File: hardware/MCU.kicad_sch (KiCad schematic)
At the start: 26 parts, among them J1 Conn_01x03_Pin, SW1 SW_MEC_5G, U1 STM32G473QETxZ, U2 IS61W204816BLL, Y1 25MHz

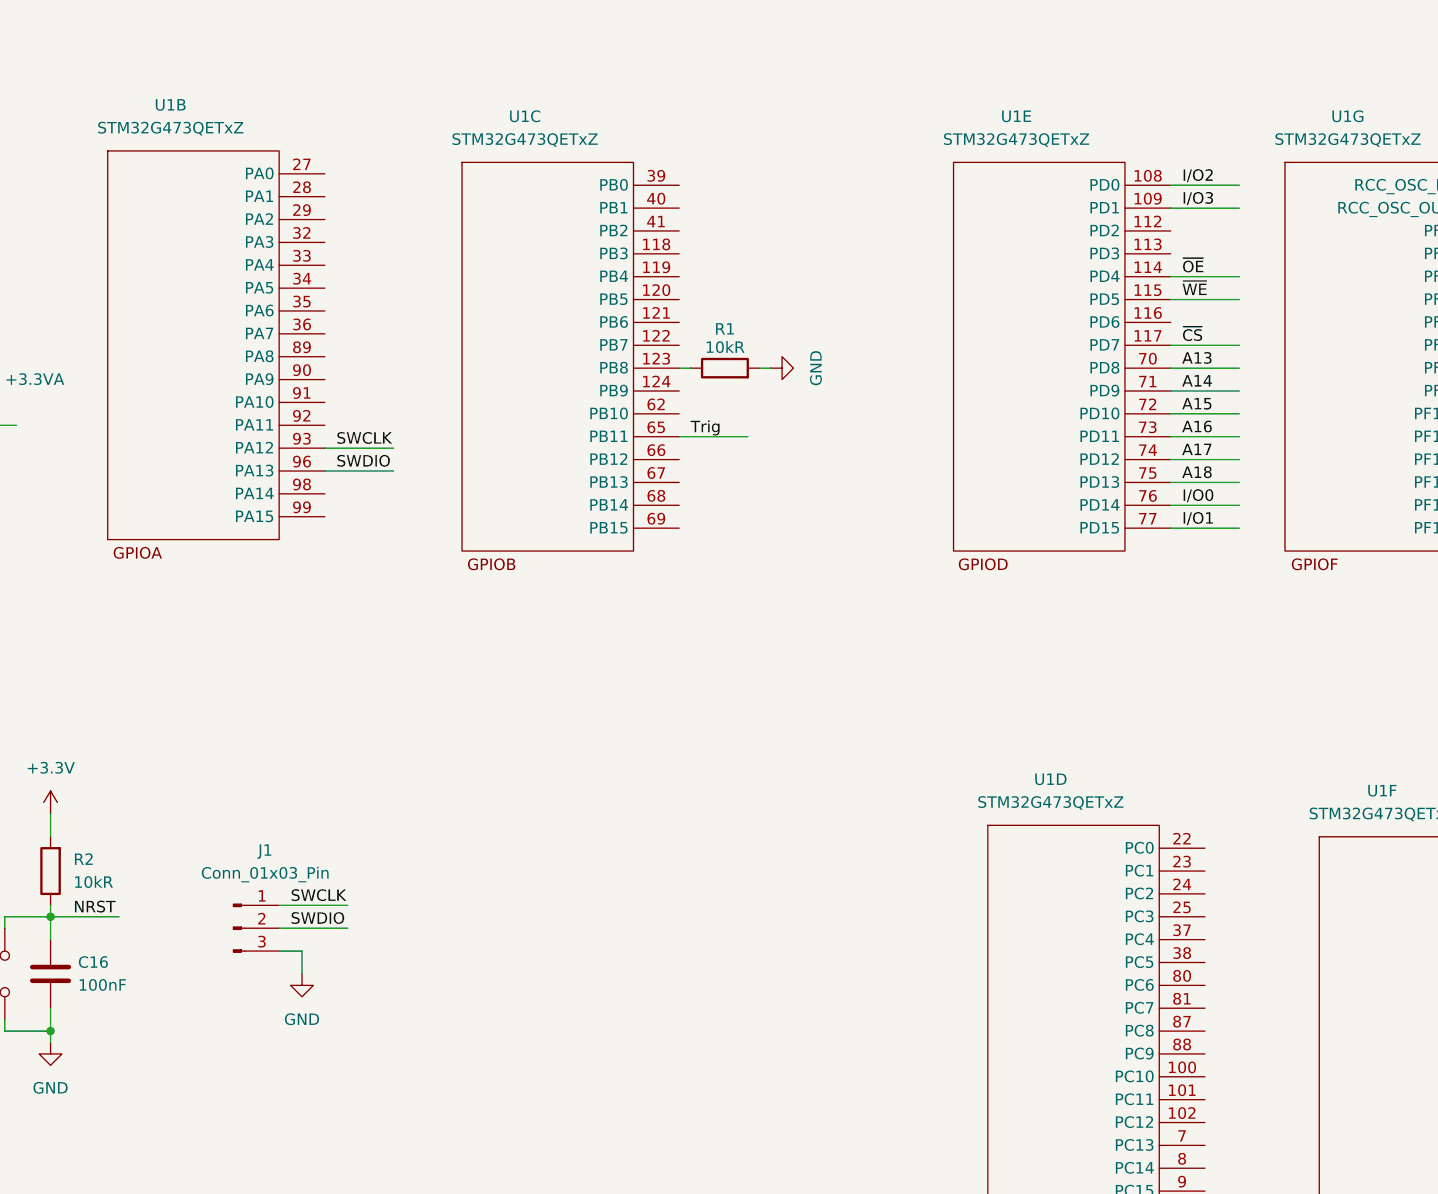
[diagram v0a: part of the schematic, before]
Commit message: feat：输入滤波原理图
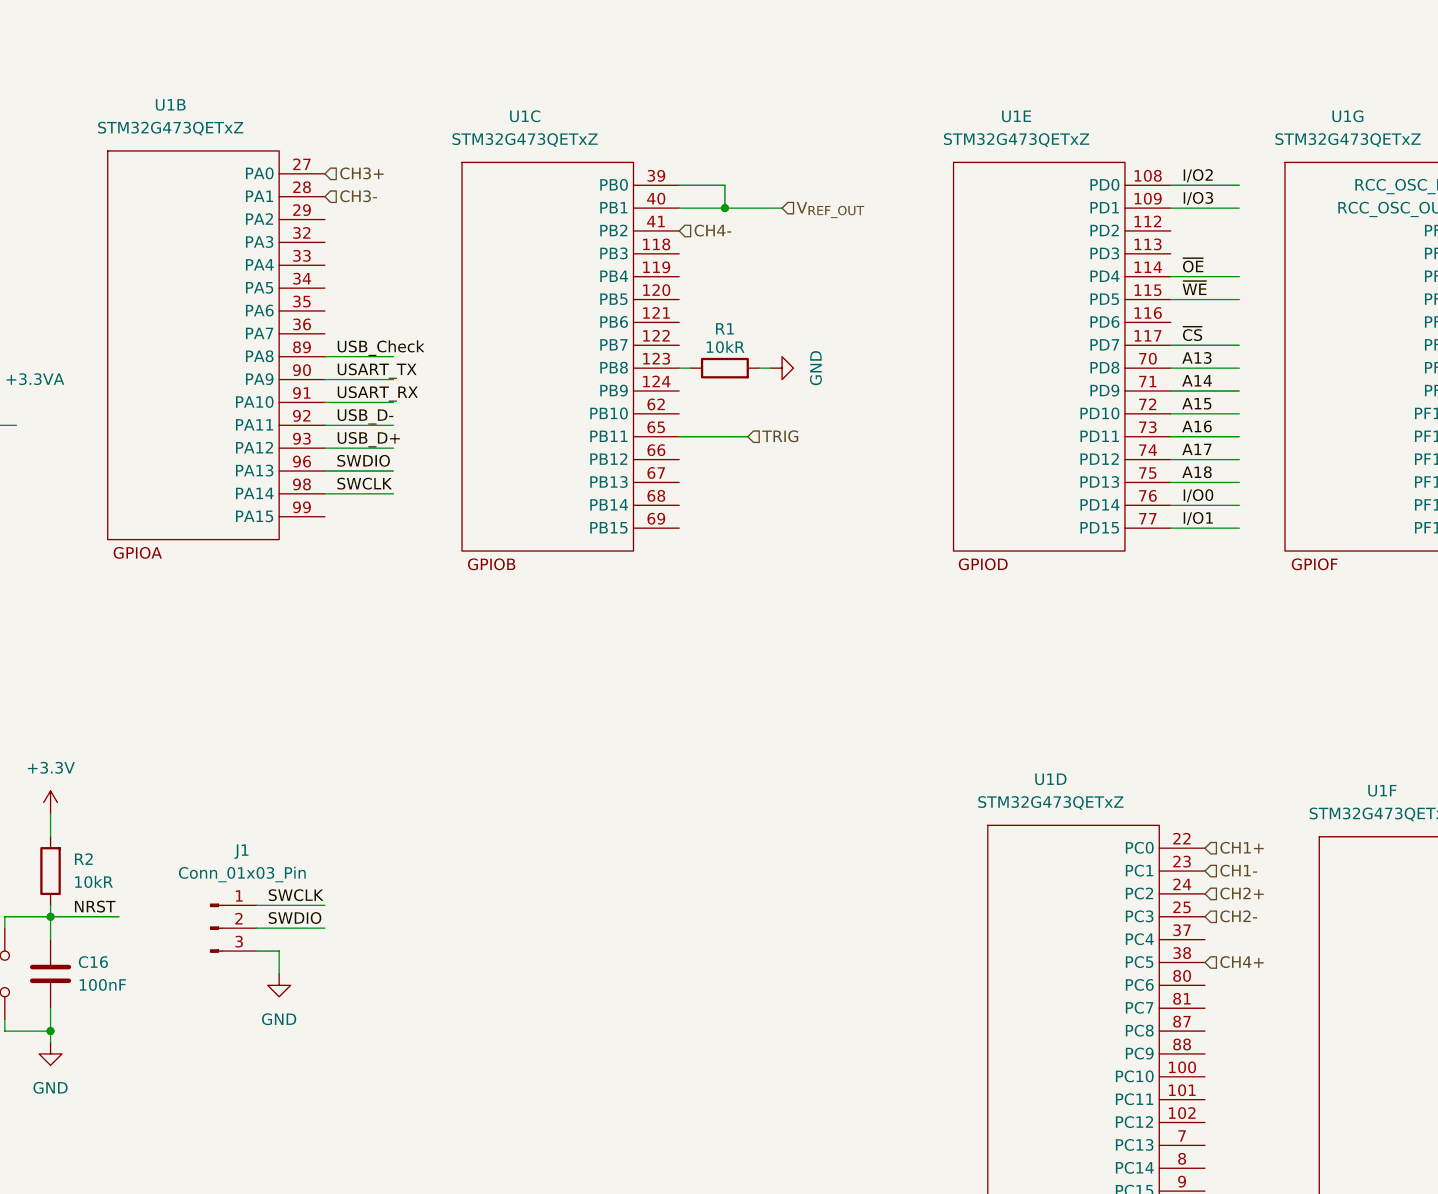
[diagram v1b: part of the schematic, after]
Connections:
- net SWCLK: now also U1.98 (PA14); no longer U1.93 (PA12)
- net CH1+: now reaches U1.22 (PC0)
- net CH1-: now reaches U1.23 (PC1)
- net CH2+: now reaches U1.24 (PC2)
- net CH2-: now reaches U1.25 (PC3)
- net CH4+: now reaches U1.38 (PC5)
- net V_{REF_OUT}: now reaches U1.39 (PB0)
- net V_{REF_OUT}: now also U1.40 (PB1)
- net CH4-: now reaches U1.41 (PB2)
- net CH3+: now reaches U1.27 (PA0)
- net CH3-: now reaches U1.28 (PA1)
- net USB_Check: now reaches U1.89 (PA8)
- net USART_TX: now reaches U1.90 (PA9)
- net USART_RX: now reaches U1.91 (PA10)
- net USB_D-: now reaches U1.92 (PA11)
- net Trig renamed TRIG
- new net USB_D+: U1.93 (PA12)
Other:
- moved on the sheet: J1

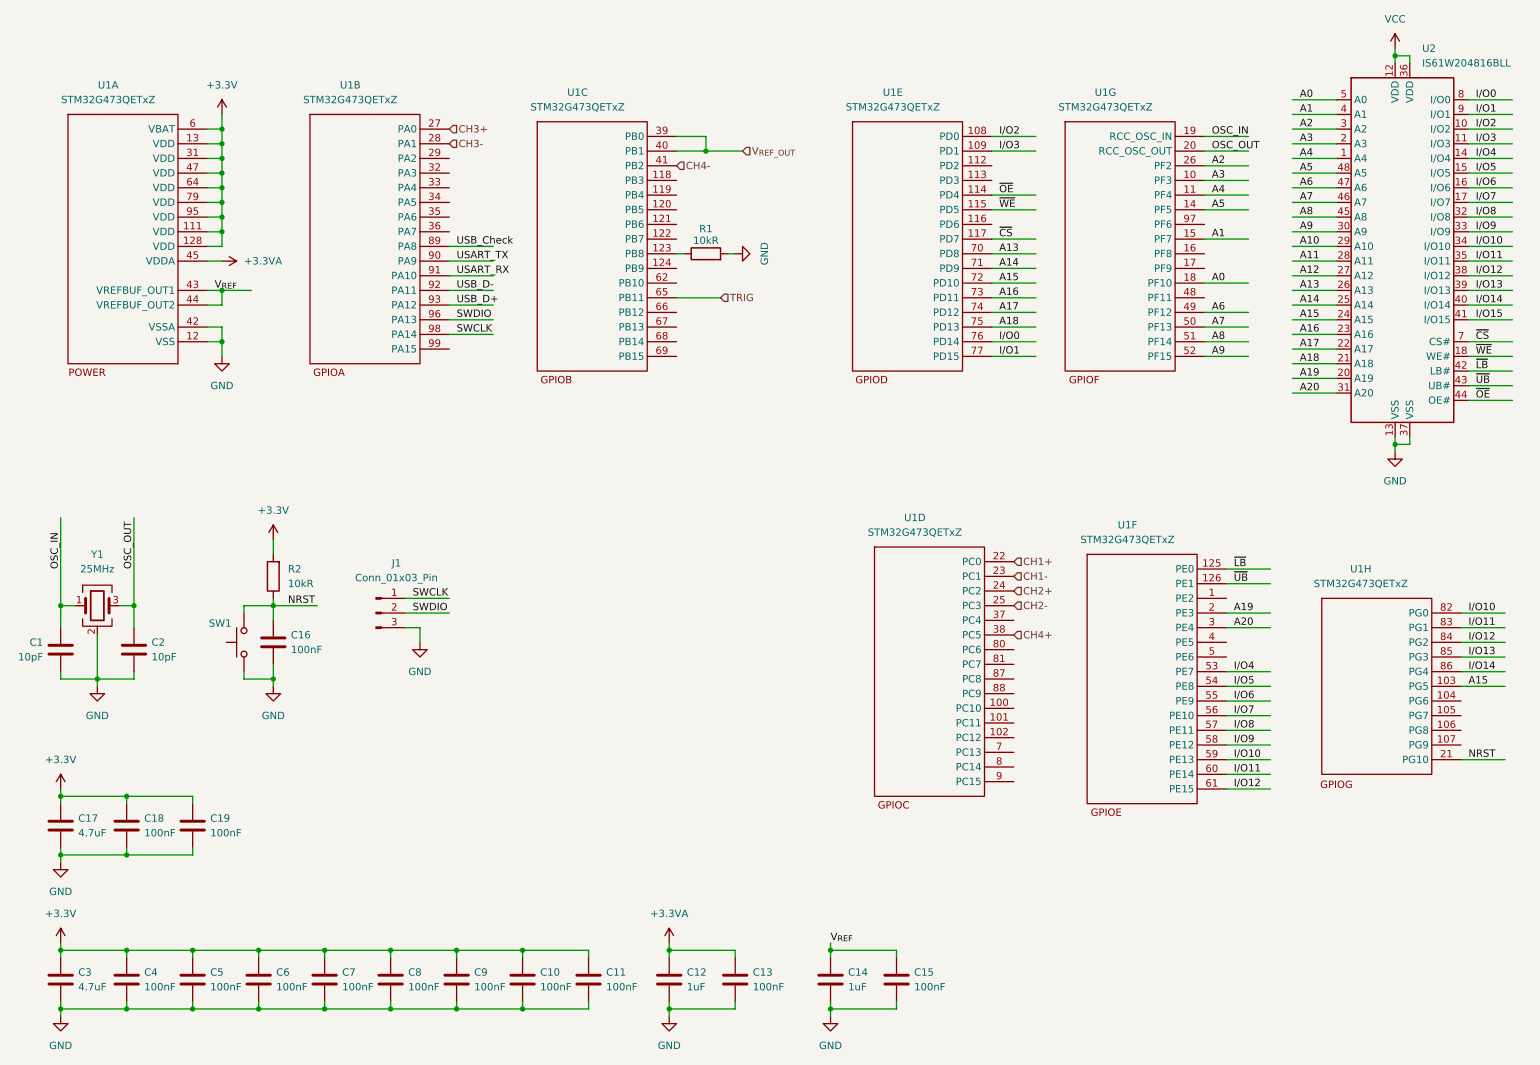
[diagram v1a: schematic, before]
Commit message: feat：电平触发原理图
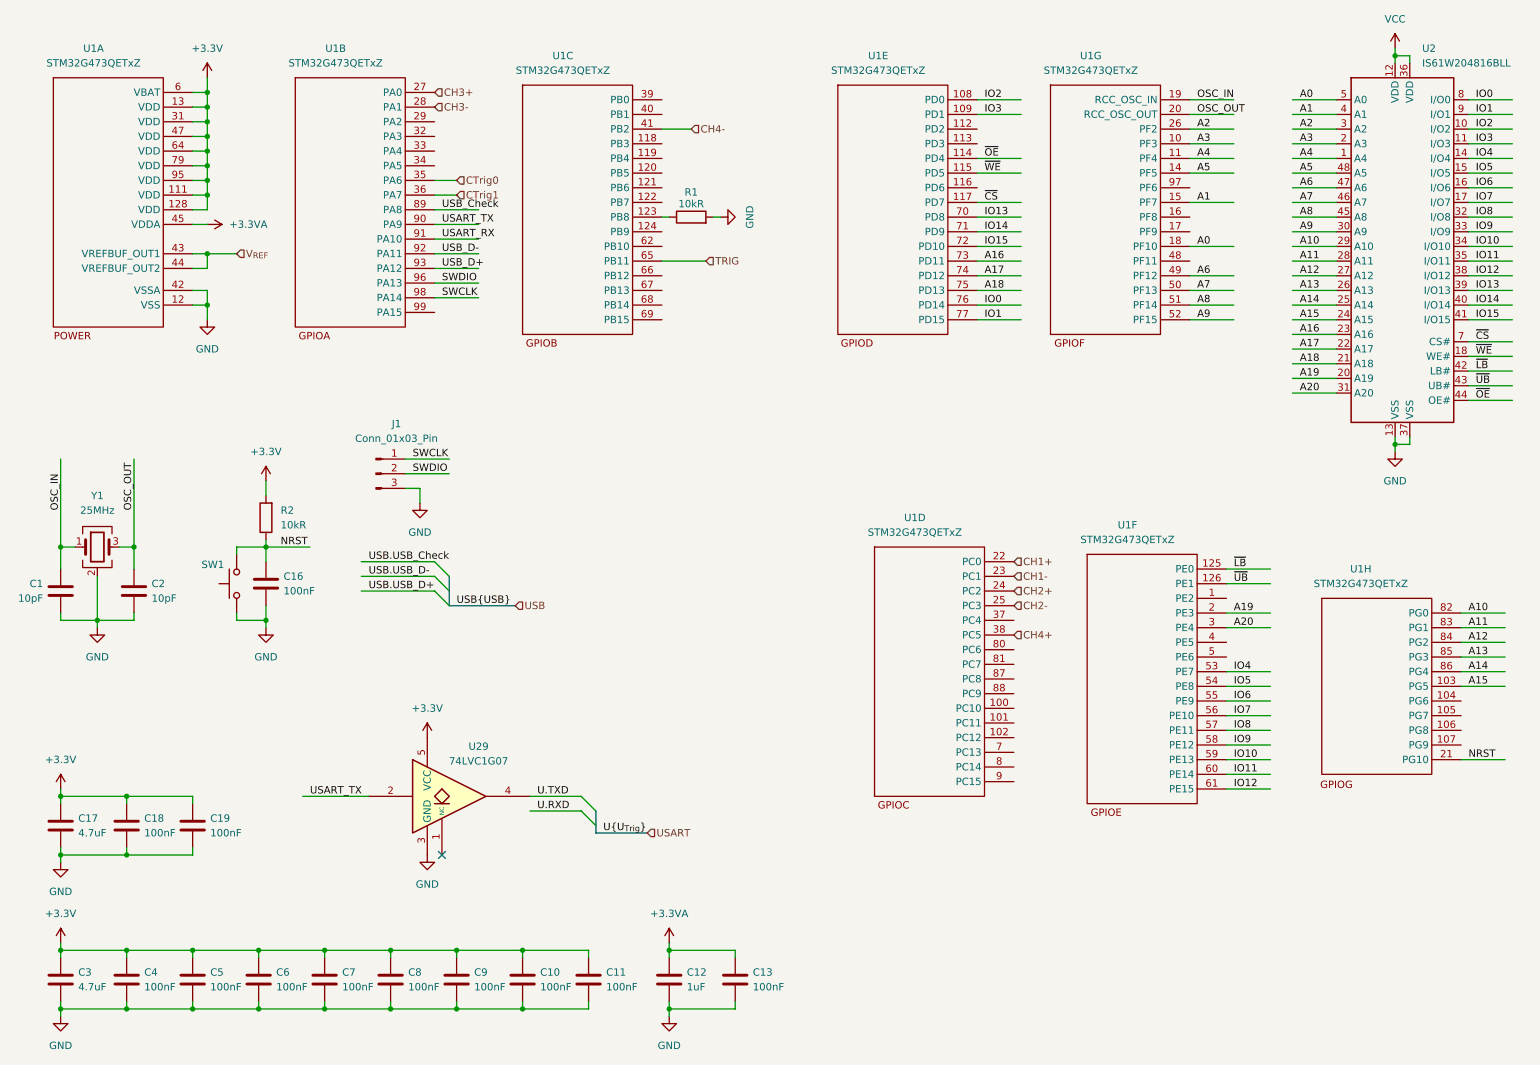
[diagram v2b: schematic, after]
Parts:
- removed C14: 1uF, Capacitor_SMD:C_0603_1608Metric, symbol Device:C
- removed C15: 100nF, Capacitor_SMD:C_0603_1608Metric, symbol Device:C
- added U29: 74LVC1G07, symbol 74xGxx:74LVC1G07
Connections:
- net +3.3V: now also U29.5 (VCC)
- net A10: now also U1.82 (PG0)
- net A11: now also U1.83 (PG1)
- net A12: now also U1.84 (PG2)
- net A13: now also U1.85 (PG3); no longer U1.70 (PD8)
- net A14: now also U1.86 (PG4); no longer U1.71 (PD9)
- net A15: no longer U1.72 (PD10)
- net GND: now also U29.3 (GND)
- net USART_TX: now also U29.2
- net CTrig0: now reaches U1.35 (PA6)
- net CTrig1: now reaches U1.36 (PA7)
- net I/O0 renamed IO0
- net I/O1 renamed IO1
- net I/O10 renamed IO10
- net IO10: no longer U1.82 (PG0)
- net I/O11 renamed IO11
- net IO11: no longer U1.83 (PG1)
- net I/O12 renamed IO12
- net IO12: no longer U1.84 (PG2)
- net I/O13 renamed IO13
- net IO13: now also U1.70 (PD8); no longer U1.85 (PG3)
- net I/O14 renamed IO14
- net IO14: now also U1.71 (PD9); no longer U1.86 (PG4)
- net I/O15 renamed IO15
- net IO15: now also U1.72 (PD10)
- net I/O2 renamed IO2
- net I/O3 renamed IO3
- net I/O4 renamed IO4
- net I/O5 renamed IO5
- net I/O6 renamed IO6
- net I/O7 renamed IO7
- net I/O8 renamed IO8
- net I/O9 renamed IO9
- net V_{REF_OUT}: no longer names the net of U1.39 (PB0)
- net V_{REF_OUT}: no longer U1.40 (PB1)
- new net U.TXD: U29.4
- no-connect marks 0 -> 1
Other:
- moved on the sheet: C1, C16, C2, J1, R1, R2, SW1, U1A, U1B, U1C, U1E, U1G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

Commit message: feat：QSPI原理图
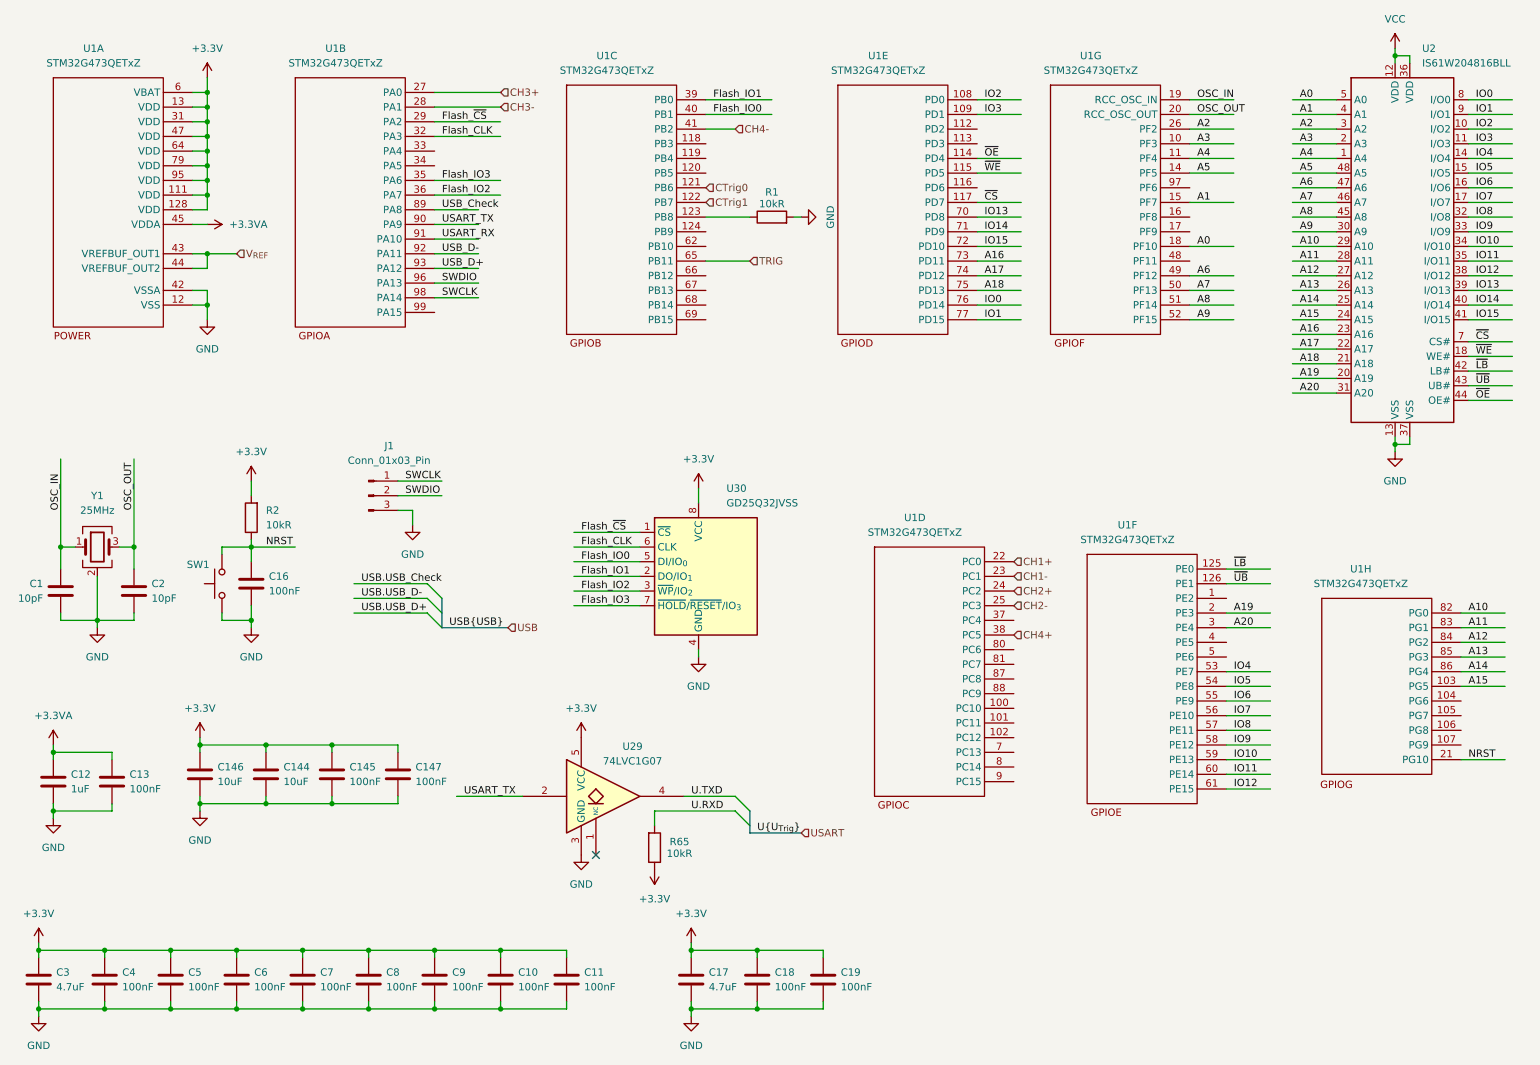
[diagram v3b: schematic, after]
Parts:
- added C144, C146: 10uF, Capacitor_SMD:C_0603_1608Metric, symbol Device:C
- added C145, C147: 100nF, Capacitor_SMD:C_0603_1608Metric, symbol Device:C
- added R65: 10kR, Resistor_SMD:R_0603_1608Metric, symbol Device:R
- added U30: GD25Q32JVSS, Package_SO:SOIC-8_5.3x5.3mm_P1.27mm, symbol Memory_Flash:GD25Q32ESIG
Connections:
- net +3.3V: now also C144.1, C145.1, C146.1, C147.1, R65.1, U30.8 (VCC)
- net CTrig0: now also U1.121 (PB6); no longer U1.35 (PA6)
- net CTrig1: now also U1.122 (PB7); no longer U1.36 (PA7)
- net GND: now also C144.2, C145.2, C146.2, C147.2, U30.4 (GND)
- net U.RXD: now also R65.2
- net Flash_IO1: now reaches U1.39 (PB0)
- net Flash_IO1: now also U30.2 (DO/IO_{1})
- net Flash_IO0: now reaches U1.40 (PB1)
- net Flash_IO0: now also U30.5 (DI/IO_{0})
- net Flash_~{CS}: now reaches U1.29 (PA2)
- net Flash_~{CS}: now also U30.1 (~{CS})
- net Flash_CLK: now reaches U1.32 (PA3)
- net Flash_CLK: now also U30.6 (CLK)
- new net Flash_IO2: U1.36 (PA7), U30.3 (~{WP}/IO_{2})
- new net Flash_IO3: U1.35 (PA6), U30.7 (~{HOLD}/~{RESET}/IO_{3})
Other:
- moved on the sheet: C10, C11, C12, C13, C16, C17, C18, C19, C3, C4, C5, C6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
